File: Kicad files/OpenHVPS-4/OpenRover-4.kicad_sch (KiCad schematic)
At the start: 69 parts, among them J1 Conn_01x03_Male, J2 Conn_01x03_Male, Q1 FQT7N10, Q2 BC846A, Q3 MMDT3906, U1 MAX6008AEUR+T, U2 74HC14, U3 MAX4162, U4 CD14538BM

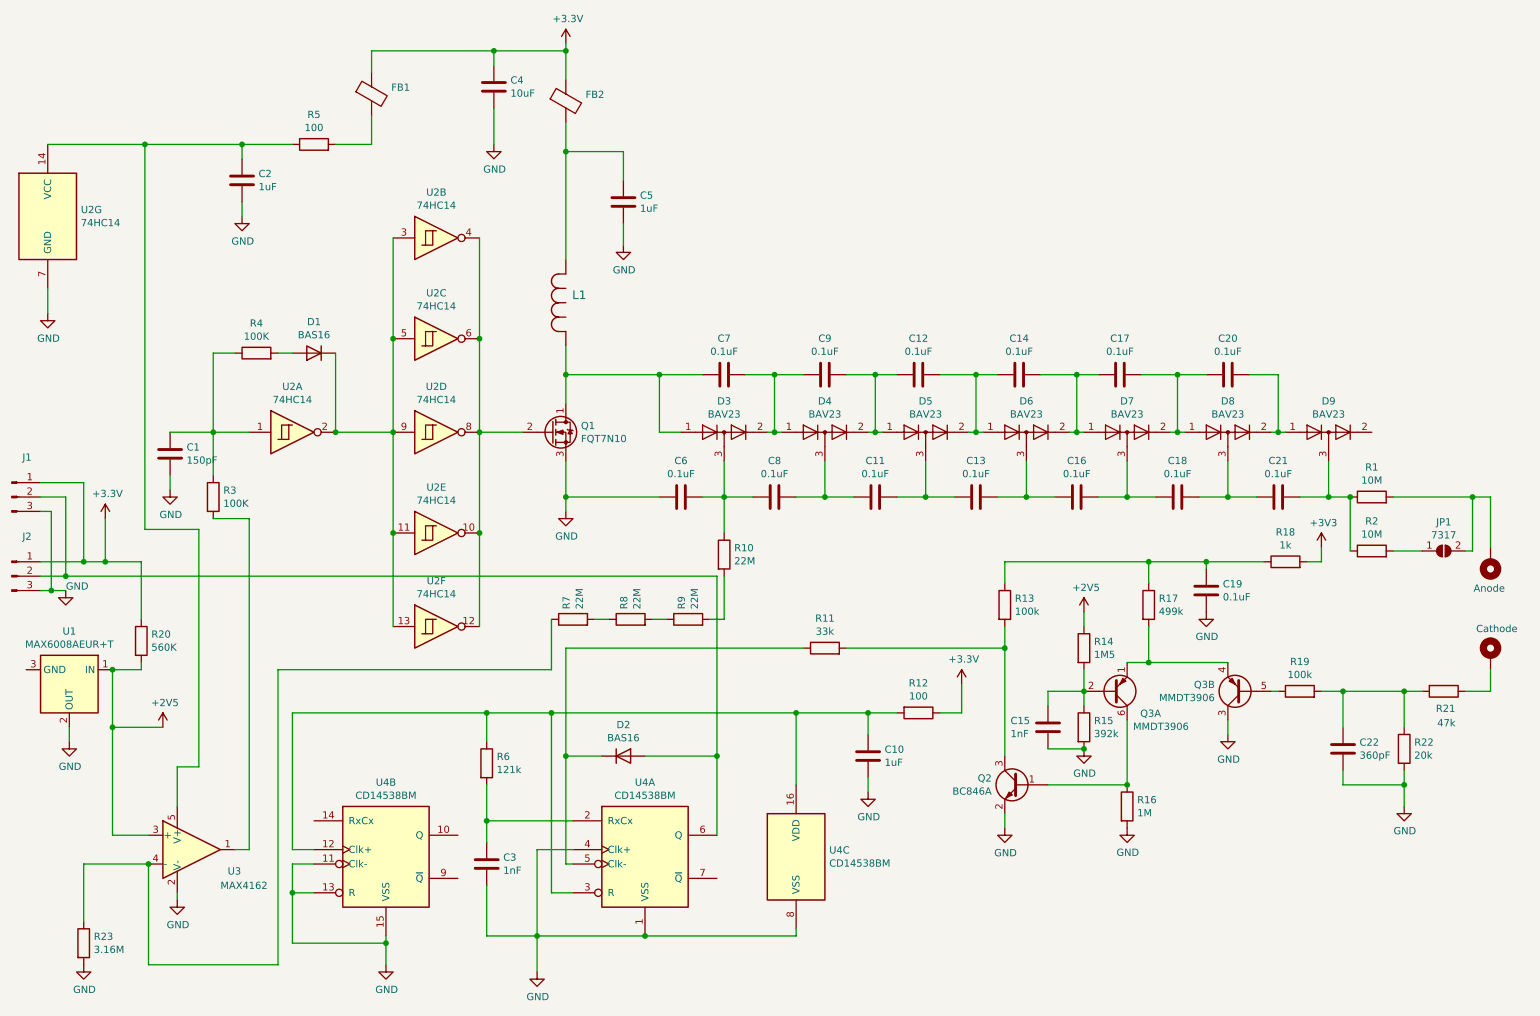
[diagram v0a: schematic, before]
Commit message: Changed D1 D2 added F1 and updated BOM
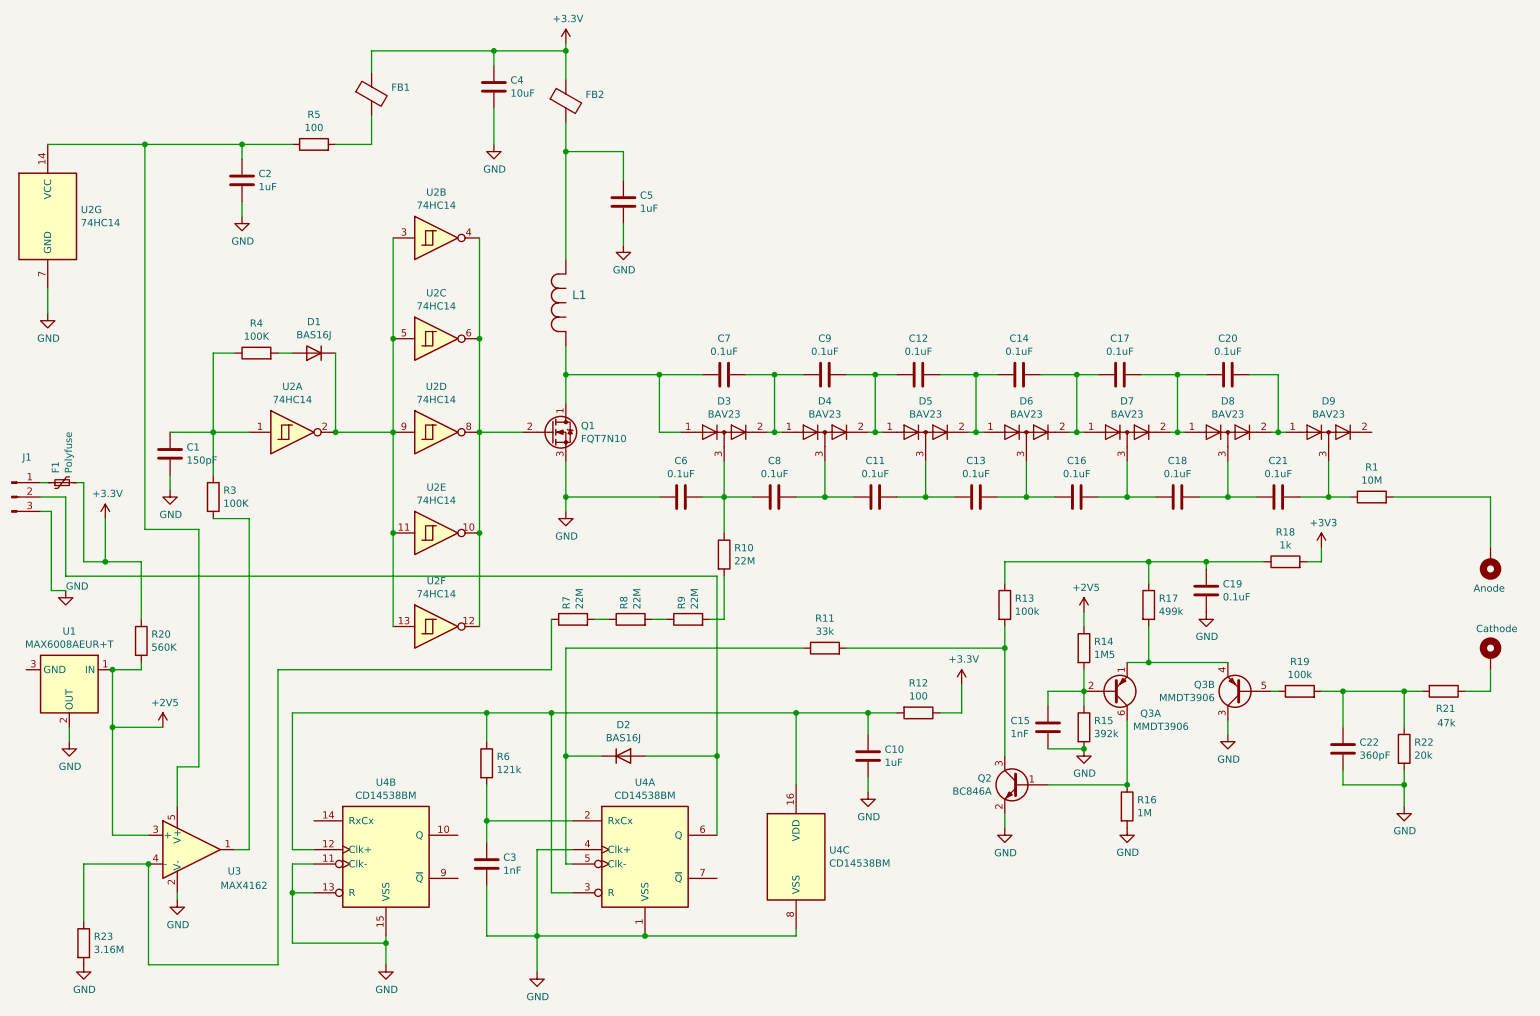
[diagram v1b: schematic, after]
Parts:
- removed J2: Conn_01x03_Male, Connector_PinHeader_2.54mm:PinHeader_1x03_P2.54mm_Vertical, symbol Connector:Conn_01x03_Male
- removed JP1: 7317, Jumper:SolderJumper-2_P1.3mm_Open_RoundedPad1.0x1.5mm, symbol Jumper:SolderJumper_2_Open
- removed R2: 10M, Resistor_SMD:R_1206_3216Metric, symbol Device:R
- added F1: Polyfuse, Resistor_SMD:R_0805_2012Metric, symbol Device:Polyfuse_Small
- D1, D2: value BAS16 -> BAS16J; footprint Diode_SMD:D_SOT-23_ANK -> Diode_SMD:D_SOD-323
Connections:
- net +3V3: now also F1.2; no longer J1.1 (Pin_1)
- new net: F1.1, J1.1 (Pin_1)
